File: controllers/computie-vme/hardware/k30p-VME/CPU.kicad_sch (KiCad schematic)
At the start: 19 parts, among them SW1 ~{RESET}, U1 MC68030FE, U2 74HC14, U3 74HC05, Y1 Crystal

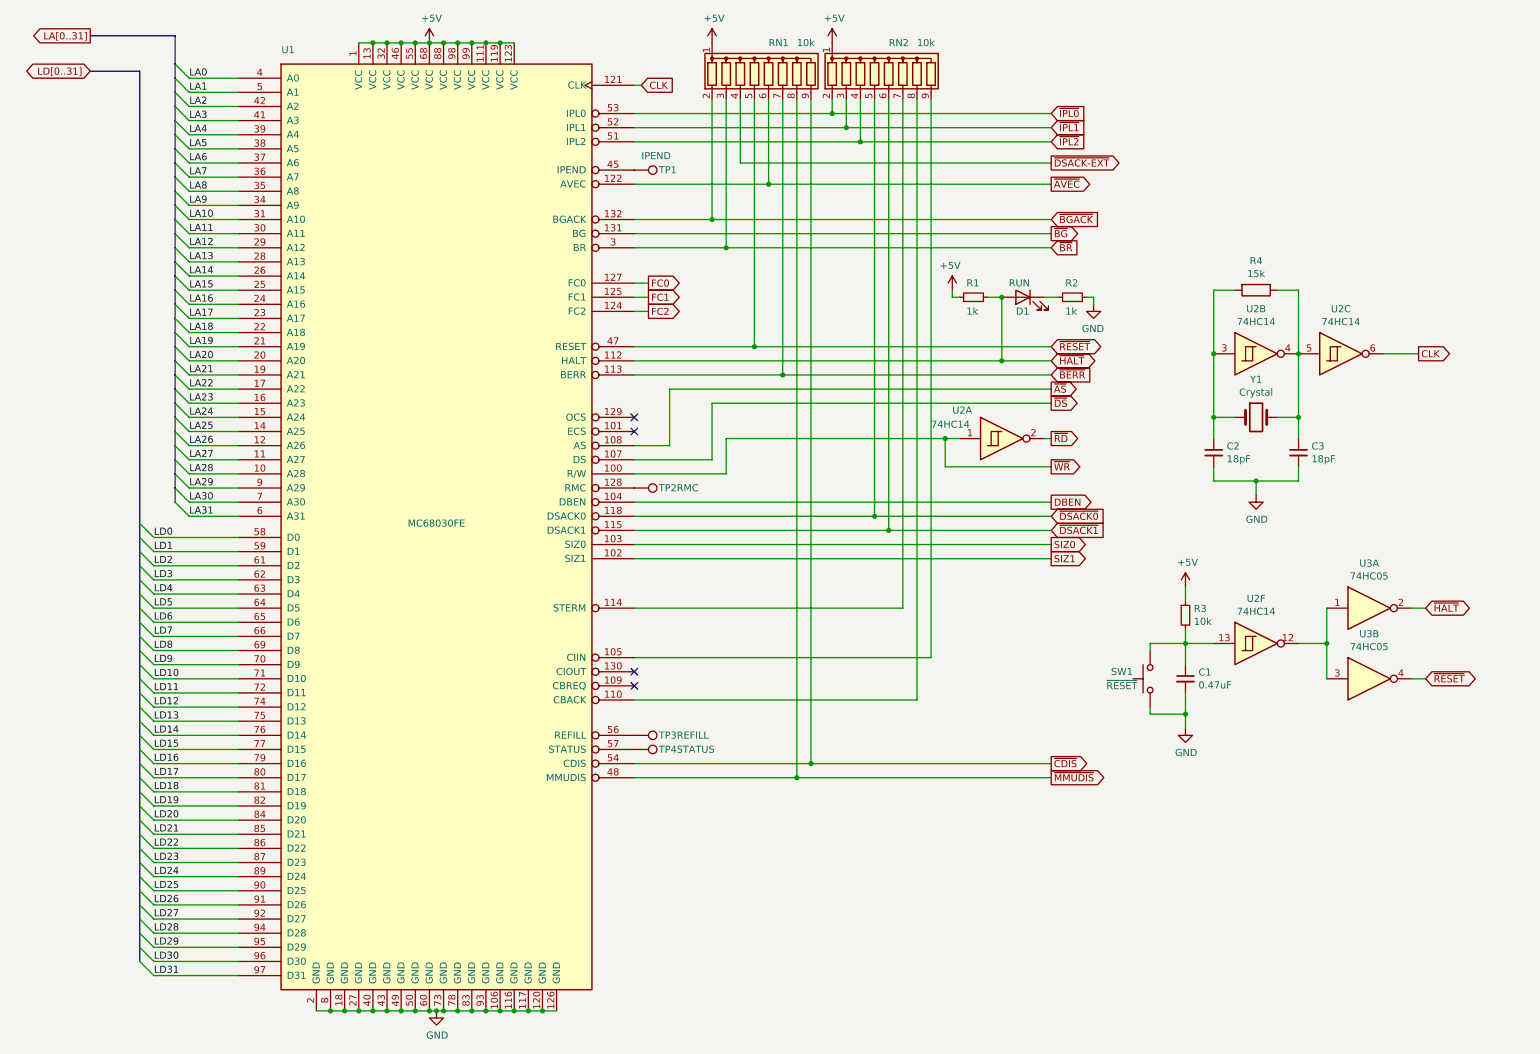
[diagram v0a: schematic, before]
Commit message: Added SystemBoardSMT, renamed k30 boards, and added progress
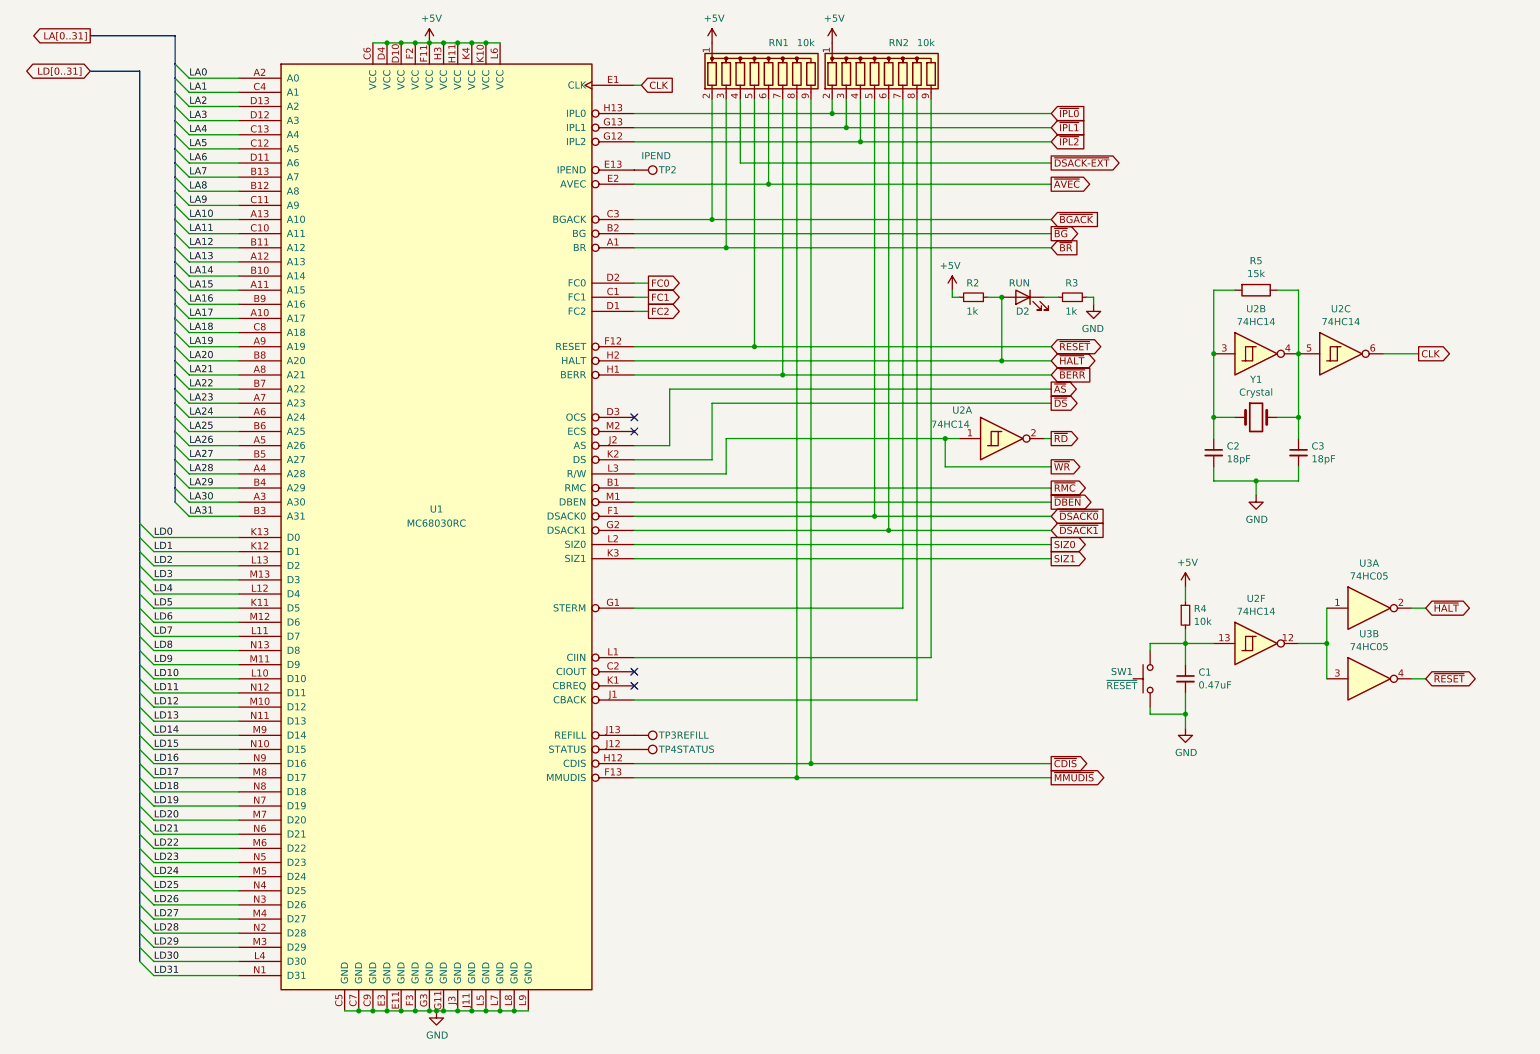
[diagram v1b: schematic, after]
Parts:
- removed TP2: RMC, TestPoint:TestPoint_THTPad_2.0x2.0mm_Drill1.0mm, symbol Connector:TestPoint
- D2: renamed from D1; footprint LED_THT:LED_D5.0mm -> LED_THT:LED_D3.0mm
- R2: renamed from R1; footprint Resistor_THT:R_Axial_DIN0204_L3.6mm_D1.6mm_P5.08mm_Horizontal -> Resistor_SMD:R_0805_2012Metric_Pad1.20x1.40mm_HandSolder
- R3: renamed from R2; footprint Resistor_THT:R_Axial_DIN0204_L3.6mm_D1.6mm_P5.08mm_Horizontal -> Resistor_SMD:R_0805_2012Metric_Pad1.20x1.40mm_HandSolder
- R4: renamed from R3; footprint Resistor_THT:R_Axial_DIN0204_L3.6mm_D1.6mm_P5.08mm_Horizontal -> Resistor_SMD:R_0805_2012Metric_Pad1.20x1.40mm_HandSolder
- R5: renamed from R4; footprint Resistor_THT:R_Axial_DIN0204_L3.6mm_D1.6mm_P5.08mm_Horizontal -> Resistor_SMD:R_0805_2012Metric_Pad1.20x1.40mm_HandSolder
- U1: value MC68030FE -> MC68030RC; footprint Package_QFP:PQFP-132_24x24mm_P0.635mm -> Computie_THT:PGA-128_13x13_THT-Socket; symbol Computie_68k:MC68030FE -> Computie_68k:MC68030RC
- renumbered TP1 to TP2
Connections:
- net +5V: now also U1.C6 (VCC), U1.D10 (VCC), U1.D4 (VCC), U1.F11 (VCC), U1.F2 (VCC), U1.H11 (VCC), U1.H3 (VCC), U1.K10 (VCC), U1.K4 (VCC), U1.L6 (VCC); no longer U1.1 (VCC), U1.111 (VCC), U1.119 (VCC), U1.123 (VCC), U1.13 (VCC), U1.32 (VCC), U1.46 (VCC), U1.55 (VCC), U1.68 (VCC), U1.88 (VCC), U1.98 (VCC), U1.99 (VCC)
- net CLK: now also U1.E1 (CLK); no longer U1.121 (CLK)
- net FC0: now also U1.D2 (FC0); no longer U1.127 (FC0)
- net FC1: now also U1.C1 (FC1); no longer U1.125 (FC1)
- net FC2: now also U1.D1 (FC2); no longer U1.124 (FC2)
- net GND: now also U1.C5 (GND), U1.C7 (GND), U1.C9 (GND), U1.E11 (GND), U1.E3 (GND), U1.F3 (GND), U1.G11 (GND), U1.G3 (GND), U1.J11 (GND), U1.J3 (GND), U1.L5 (GND), U1.L7 (GND), U1.L8 (GND), U1.L9 (GND); no longer U1.106 (GND), U1.116 (GND), U1.117 (GND), U1.120 (GND), U1.126 (GND), U1.18 (GND), U1.2 (GND), U1.27 (GND), U1.40 (GND), U1.43 (GND), U1.49 (GND), U1.50 (GND), U1.60 (GND), U1.73 (GND), U1.78 (GND), U1.8 (GND), U1.83 (GND), U1.93 (GND)
- net LA0: now also U1.A2 (A0); no longer U1.4 (A0)
- net LA1: now also U1.C4 (A1); no longer U1.5 (A1)
- net LA10: now also U1.A13 (A10); no longer U1.31 (A10)
- net LA11: now also U1.C10 (A11); no longer U1.30 (A11)
- net LA12: now also U1.B11 (A12); no longer U1.29 (A12)
- net LA13: now also U1.A12 (A13); no longer U1.28 (A13)
- net LA14: now also U1.B10 (A14); no longer U1.26 (A14)
- net LA15: now also U1.A11 (A15); no longer U1.25 (A15)
- net LA16: now also U1.B9 (A16); no longer U1.24 (A16)
- net LA17: now also U1.A10 (A17); no longer U1.23 (A17)
- net LA18: now also U1.C8 (A18); no longer U1.22 (A18)
- net LA19: now also U1.A9 (A19); no longer U1.21 (A19)
- net LA2: now also U1.D13 (A2); no longer U1.42 (A2)
- net LA20: now also U1.B8 (A20); no longer U1.20 (A20)
- net LA21: now also U1.A8 (A21); no longer U1.19 (A21)
- net LA22: now also U1.B7 (A22); no longer U1.17 (A22)
- net LA23: now also U1.A7 (A23); no longer U1.16 (A23)
- net LA24: now also U1.A6 (A24); no longer U1.15 (A24)
- net LA25: now also U1.B6 (A25); no longer U1.14 (A25)
- net LA26: now also U1.A5 (A26); no longer U1.12 (A26)
- net LA27: now also U1.B5 (A27); no longer U1.11 (A27)
- net LA28: now also U1.A4 (A28); no longer U1.10 (A28)
- net LA29: now also U1.B4 (A29); no longer U1.9 (A29)
- net LA3: now also U1.D12 (A3); no longer U1.41 (A3)
- net LA30: now also U1.A3 (A30); no longer U1.7 (A30)
- net LA31: now also U1.B3 (A31); no longer U1.6 (A31)
- net LA4: now also U1.C13 (A4); no longer U1.39 (A4)
- net LA5: now also U1.C12 (A5); no longer U1.38 (A5)
- net LA6: now also U1.D11 (A6); no longer U1.37 (A6)
- net LA7: now also U1.B13 (A7); no longer U1.36 (A7)
- net LA8: now also U1.B12 (A8); no longer U1.35 (A8)
- net LA9: now also U1.C11 (A9); no longer U1.34 (A9)
- net LD0: now also U1.K13 (D0); no longer U1.58 (D0)
- net LD1: now also U1.K12 (D1); no longer U1.59 (D1)
- net LD10: now also U1.L10 (D10); no longer U1.71 (D10)
- net LD11: now also U1.N12 (D11); no longer U1.72 (D11)
- net LD12: now also U1.M10 (D12); no longer U1.74 (D12)
- net LD13: now also U1.N11 (D13); no longer U1.75 (D13)
- net LD14: now also U1.M9 (D14); no longer U1.76 (D14)
- net LD15: now also U1.N10 (D15); no longer U1.77 (D15)
- net LD16: now also U1.N9 (D16); no longer U1.79 (D16)
- net LD17: now also U1.M8 (D17); no longer U1.80 (D17)
- net LD18: now also U1.N8 (D18); no longer U1.81 (D18)
- net LD19: now also U1.N7 (D19); no longer U1.82 (D19)
- net LD2: now also U1.L13 (D2); no longer U1.61 (D2)
- net LD20: now also U1.M7 (D20); no longer U1.84 (D20)
- net LD21: now also U1.N6 (D21); no longer U1.85 (D21)
- net LD22: now also U1.M6 (D22); no longer U1.86 (D22)
- net LD23: now also U1.N5 (D23); no longer U1.87 (D23)
- net LD24: now also U1.M5 (D24); no longer U1.89 (D24)
- net LD25: now also U1.N4 (D25); no longer U1.90 (D25)
- net LD26: now also U1.N3 (D26); no longer U1.91 (D26)
- net LD27: now also U1.M4 (D27); no longer U1.92 (D27)
- net LD28: now also U1.N2 (D28); no longer U1.94 (D28)
- net LD29: now also U1.M3 (D29); no longer U1.95 (D29)
- net LD3: now also U1.M13 (D3); no longer U1.62 (D3)
- net LD30: now also U1.L4 (D30); no longer U1.96 (D30)
- net LD31: now also U1.N1 (D31); no longer U1.97 (D31)
- net LD4: now also U1.L12 (D4); no longer U1.63 (D4)
- net LD5: now also U1.K11 (D5); no longer U1.64 (D5)
- net LD6: now also U1.M12 (D6); no longer U1.65 (D6)
- net LD7: now also U1.L11 (D7); no longer U1.66 (D7)
- net LD8: now also U1.N13 (D8); no longer U1.69 (D8)
- net LD9: now also U1.M11 (D9); no longer U1.70 (D9)
- net SIZ0: now also U1.L2 (SIZ0); no longer U1.103 (SIZ0)
- net SIZ1: now also U1.K3 (SIZ1); no longer U1.102 (SIZ1)
- net ~{AS}: now also U1.J2 (AS); no longer U1.108 (AS)
- net ~{AVEC}: now also U1.E2 (AVEC); no longer U1.122 (AVEC)
- net ~{BERR}: now also U1.H1 (BERR); no longer U1.113 (BERR)
- net ~{BGACK}: now also U1.C3 (BGACK); no longer U1.132 (BGACK)
- net ~{BG}: now also U1.B2 (BG); no longer U1.131 (BG)
- net ~{BR}: now also U1.A1 (BR); no longer U1.3 (BR)
- net ~{CDIS}: now also U1.H12 (CDIS); no longer U1.54 (CDIS)
- net ~{DSACK0}: now also U1.F1 (DSACK0); no longer U1.118 (DSACK0)
- net ~{DSACK1}: now also U1.G2 (DSACK1); no longer U1.115 (DSACK1)
- net ~{DS}: now also U1.K2 (DS); no longer U1.107 (DS)
- net ~{HALT}: now also U1.H2 (HALT); no longer U1.112 (HALT)
- net ~{IPL0}: now also U1.H13 (IPL0); no longer U1.53 (IPL0)
- net ~{IPL1}: now also U1.G13 (IPL1); no longer U1.52 (IPL1)
- net ~{IPL2}: now also U1.G12 (IPL2); no longer U1.51 (IPL2)
- net ~{MMUDIS}: now also U1.F13 (MMUDIS); no longer U1.48 (MMUDIS)
- net ~{RESET}: now also U1.F12 (RESET); no longer U1.47 (RESET)
- net ~{WR}: now also U1.L3 (R/W); no longer U1.100 (R/W)
- net at RN2.7 (R6): now also U1.G1 (STERM); no longer U1.114 (STERM)
- net at RN2.8 (R7): now also U1.J1 (CBACK); no longer U1.110 (CBACK)
- net at RN2.9 (R8): now also U1.L1 (CIIN); no longer U1.105 (CIIN)
- net at TP2.1: now also U1.E13 (IPEND); no longer U1.45 (IPEND)
- net at TP3.1: now also U1.J13 (REFILL); no longer U1.56 (REFILL)
- net at TP4.1: now also U1.J12 (STATUS); no longer U1.57 (STATUS)
- removed net DBEN: U1.104 (DBEN)
- new net ~{DBEN}: U1.M1 (DBEN)
- new net ~{RMC}: U1.B1 (RMC)

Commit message: Updating with more work in progress
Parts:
- removed D2: RUN, LED_THT:LED_D3.0mm, symbol Device:LED
- added D1: Harvatek HV-32H307B, Computie_Miscellaneous:Harvatek_HV-32312-260-2SUB, symbol Device:LED_Dual_AKAK
- added JP1: CDIS, Connector_PinHeader_2.54mm:PinHeader_1x02_P2.54mm_Vertical, symbol Jumper:Jumper_2_Open
- added JP2: MMUDIS, Connector_PinHeader_2.54mm:PinHeader_1x02_P2.54mm_Vertical, symbol Jumper:Jumper_2_Open
- added R2: 220, Resistor_SMD:R_0805_2012Metric_Pad1.20x1.40mm_HandSolder, symbol Device:R_Small
- C1: footprint Capacitor_THT:C_Disc_D3.0mm_W2.0mm_P2.50mm -> Capacitor_SMD:C_0805_2012Metric_Pad1.18x1.45mm_HandSolder
- SW1: footprint Button_Switch_THT:SW_PUSH_6mm -> Computie_Miscellaneous:E-Switch_TL1105
- renumbered R2 to R1
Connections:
- net GND: now also JP1.2 (B), JP2.2 (B), R2.1
- net ~{AVEC}: now also RN1.3 (R2); no longer RN1.6 (R5)
- net ~{BERR}: now also RN1.4 (R3); no longer RN1.7 (R6)
- net ~{BR}: now also RN2.2 (R1); no longer RN1.3 (R2)
- net ~{CDIS}: now also RN2.9 (R8), JP1.1 (A); no longer RN1.9 (R8)
- net ~{DSACK-EXT}: now also RN2.3 (R2); no longer RN1.4 (R3)
- net ~{DSACK0}: now also RN1.5 (R4); no longer RN2.5 (R4)
- net ~{DSACK1}: now also RN1.6 (R5); no longer RN2.6 (R5)
- net ~{HALT}: now also D1.1 (A1)
- net ~{IPL0}: now also RN2.5 (R4); no longer RN2.2 (R1)
- net ~{IPL1}: now also RN2.6 (R5); no longer RN2.3 (R2)
- net ~{IPL2}: now also RN2.7 (R6); no longer RN2.4 (R3)
- net ~{MMUDIS}: now also RN2.8 (R7), JP2.1 (A); no longer RN1.8 (R7)
- net ~{RESET}: now also RN2.4 (R3); no longer RN1.5 (R4)
- net at U1.G1 (STERM): now also RN1.7 (R6); no longer RN2.7 (R6)
- net at U1.J1 (CBACK): now also RN1.8 (R7); no longer RN2.8 (R7)
- net at U1.L1 (CIIN): now also RN1.9 (R8); no longer RN2.9 (R8)
- net at R3.2: now also D1.2 (K1)
- new net: D1.4 (K2), R2.2
- new net STATUSLED: D1.3 (A2)
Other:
- note added: "CONFIGURATION JUMPERS"
- note added: "POWER-ON RESET"
- note added: "PRIMARY CLOCK"
- title: k30-VME32 -> k30p-VME
- moved on the sheet: C1, C2, C3, R1, R3, R4, R5, SW1, U2B, U2C, U2F, U3A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

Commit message: Reorganized a bit
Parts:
- removed C2, C3: 18pF, Capacitor_THT:C_Disc_D3.0mm_W2.0mm_P2.50mm, symbol Device:C_Small
- removed R5: 15k, Resistor_SMD:R_0805_2012Metric_Pad1.20x1.40mm_HandSolder, symbol Device:R
- removed unit 2 of U2
- removed unit 3 of U2
- removed Y1: Crystal, Crystal:Crystal_HC49-4H_Vertical, symbol Device:Crystal
- added JP8: SUSPEND, Connector_PinHeader_2.54mm:PinHeader_1x02_P2.54mm_Vertical, symbol Jumper:Jumper_2_Open
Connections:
- net GND: now also JP8.2 (B)
- net ~{BR}: now also JP8.1 (A)
- net CLK renamed CPU_CLK
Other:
- note removed: "PRIMARY CLOCK"

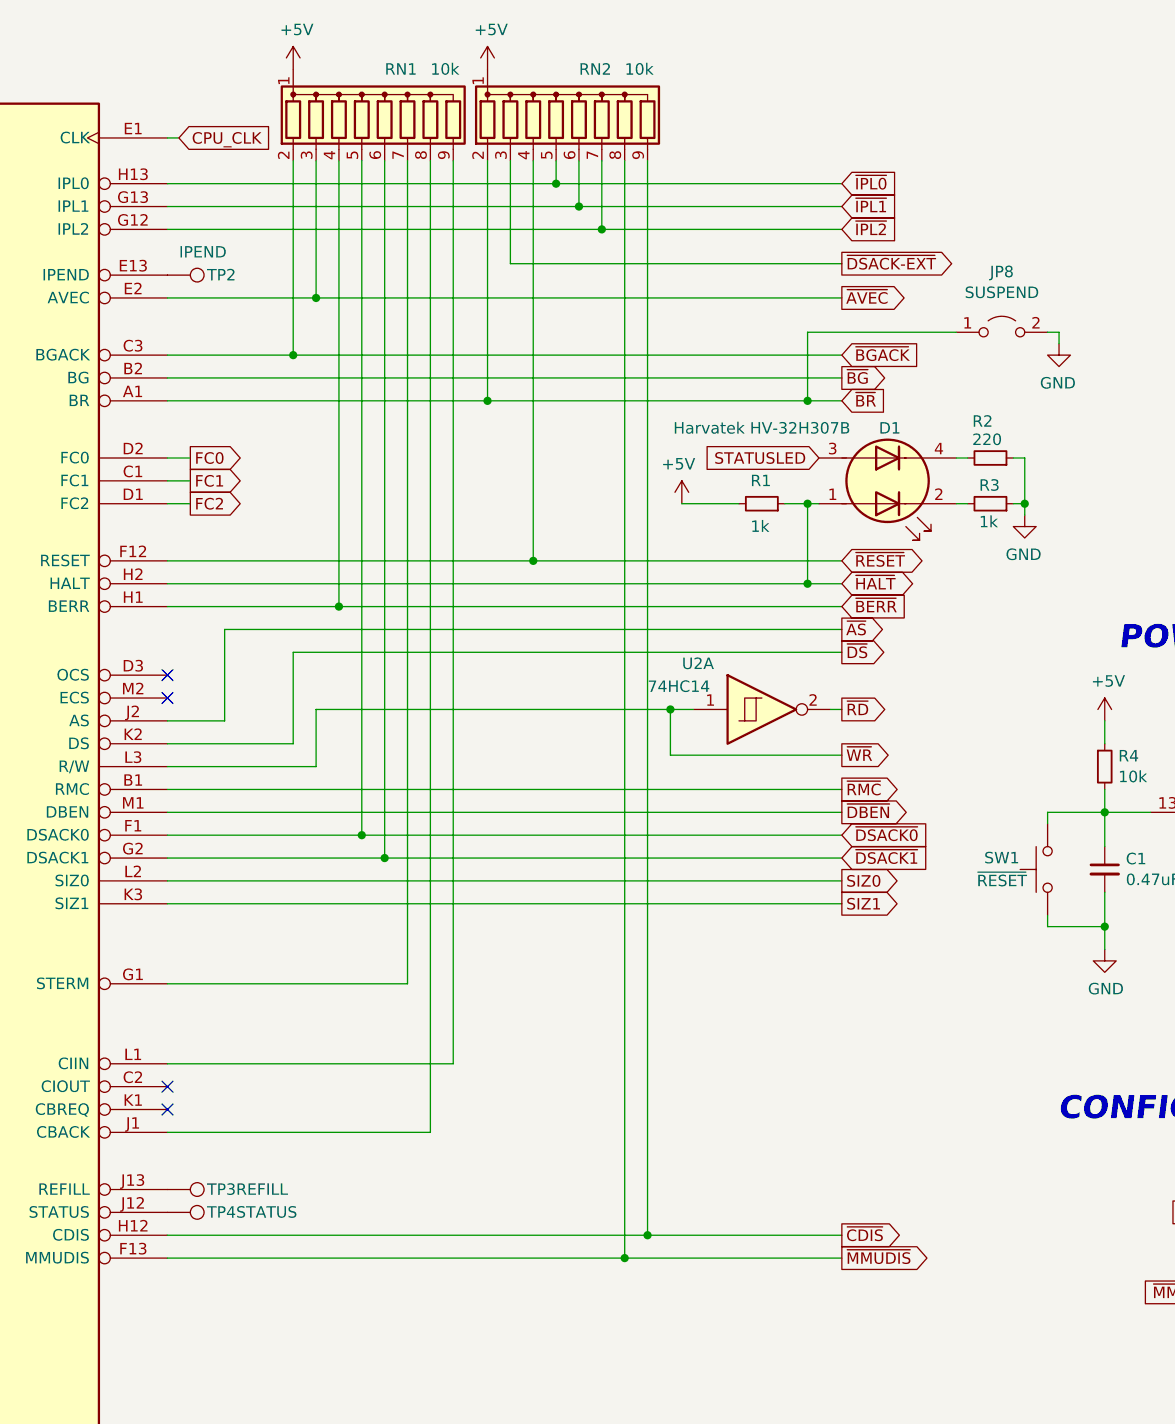
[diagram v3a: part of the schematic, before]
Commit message: Basic systemboard logic for bus arbitration is working and tested
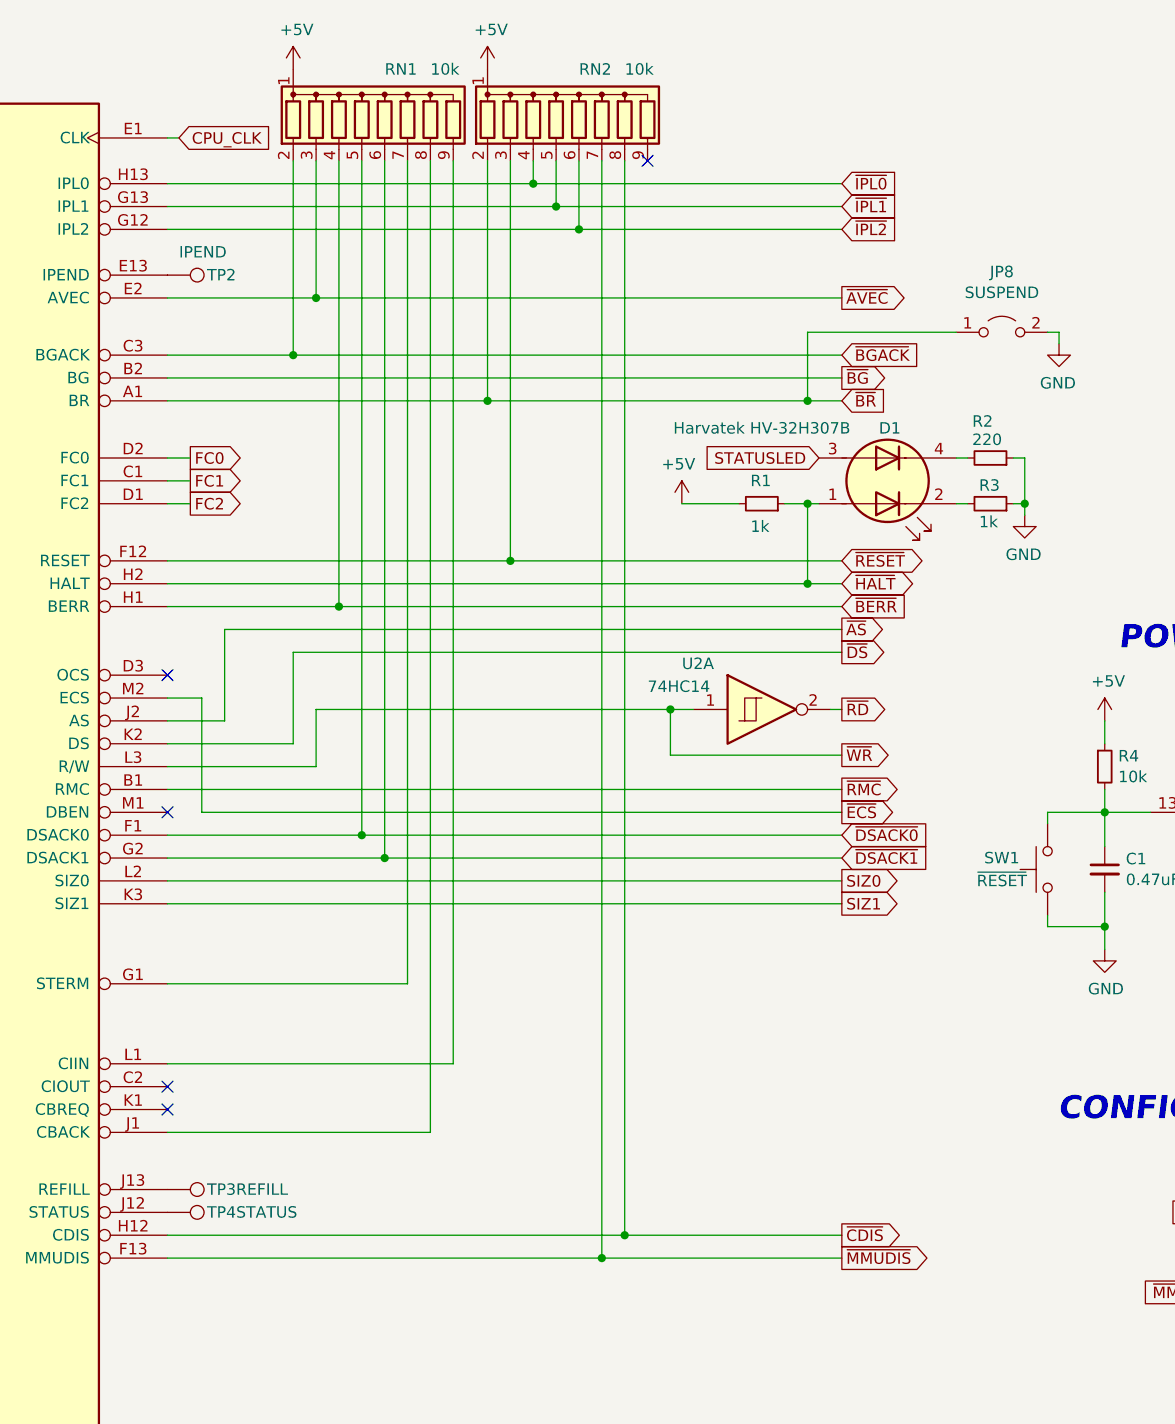
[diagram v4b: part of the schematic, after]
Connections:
- net ~{DSACK-EXT} is gone; now on net ~{RESET}: RN2.3 (R2)
- net ~{CDIS}: now also RN2.8 (R7); no longer RN2.9 (R8)
- net ~{IPL0}: now also RN2.4 (R3); no longer RN2.5 (R4)
- net ~{IPL1}: now also RN2.5 (R4); no longer RN2.6 (R5)
- net ~{IPL2}: now also RN2.6 (R5); no longer RN2.7 (R6)
- net ~{MMUDIS}: now also RN2.7 (R6); no longer RN2.8 (R7)
- net ~{RESET}: no longer RN2.4 (R3)
- net ~{ECS}: now reaches U1.M2 (ECS)
- net ~{DBEN}: no longer names the net of U1.M1 (DBEN)
- no-connect marks 4 -> 5
